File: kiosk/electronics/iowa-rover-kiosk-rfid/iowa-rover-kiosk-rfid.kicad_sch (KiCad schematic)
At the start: 6 parts, among them J1 Conn_01x04, J2 Conn_01x04, U1 ID12-LA, U2 ATtiny84-20P

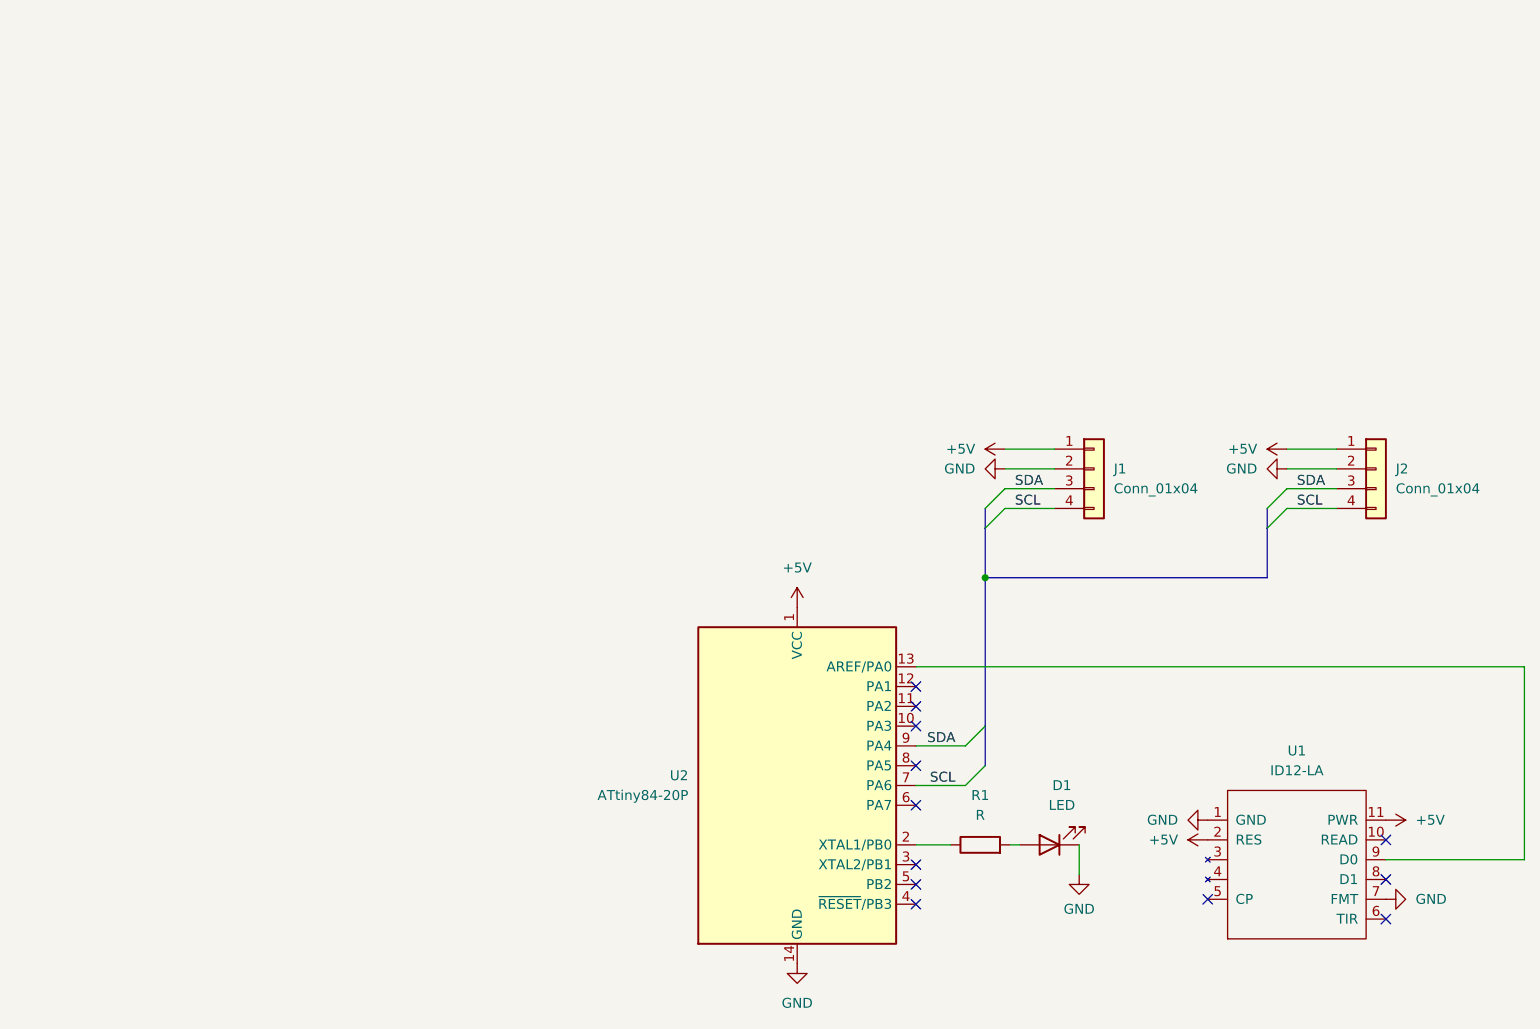
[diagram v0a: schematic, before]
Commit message: initial pass at board drawings
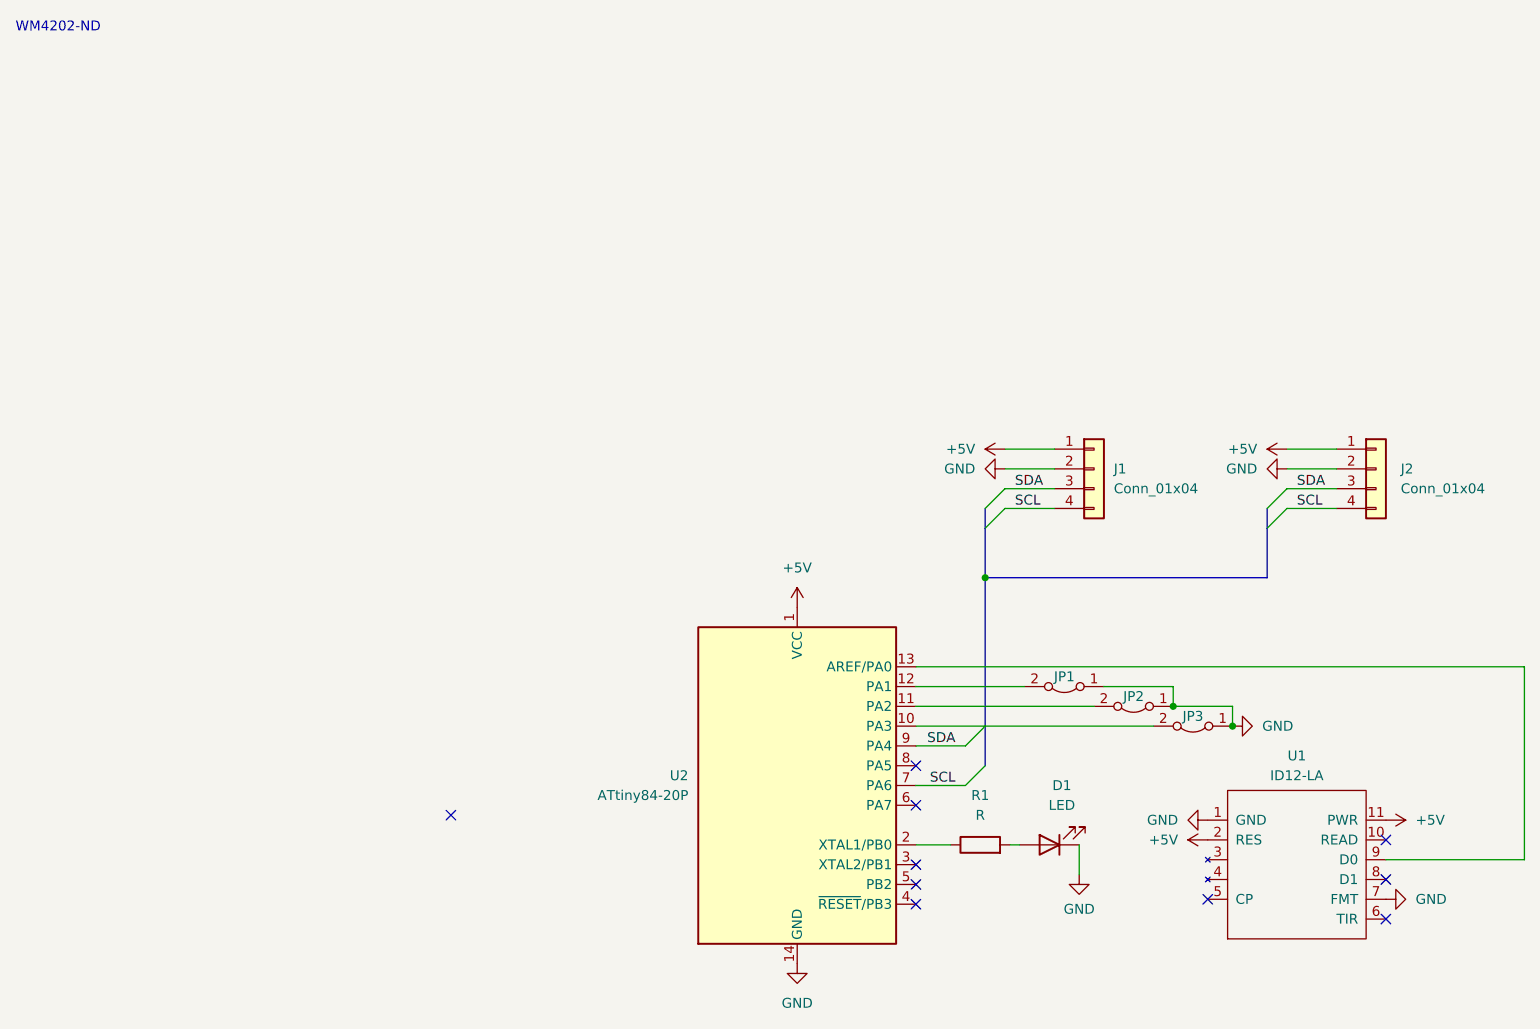
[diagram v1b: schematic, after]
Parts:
- added JP1, JP2, JP3: Jumper_2_Bridged, Jumper:SolderJumper-2_P1.3mm_Bridged_RoundedPad1.0x1.5mm, symbol Jumper:Jumper_2_Bridged
- D1: footprint (none) -> SMM:LED_D3.0mm
- J1, J2: footprint (none) -> SMM:KK-1x04
- R1: footprint (none) -> SMM:Resistor_L6.3mm_D2.5mm_P10.16mm_Horizontal
- U1: footprint (none) -> SMM:ID-12LA-Inverted
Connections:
- net GND: now also JP1.1 (A), JP2.1 (A), JP3.1 (A)
- net at U2.10 (PA3): now also JP3.2 (B)
- net at U2.11 (PA2): now also JP2.2 (B)
- net at U2.12 (PA1): now also JP1.2 (B)
- no-connect marks 12 -> 10
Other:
- note added: "WM4202-ND"
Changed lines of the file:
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@@
   (junction (at 124.46 72.39) (diameter 0) (color 0 0 0 0)
+  )
+  (junction (at 148.59 88.9) (diameter 0) (color 0 0 0 0)
+  )
+  (junction (at 156.21 91.44) (diameter 0) (color 0 0 0 0)
   )
   (no_connect (at 115.57 101.6))
@@
   (no_connect (at 175.895 116.205))
   (no_connect (at 115.57 109.22))
-  (no_connect (at 115.57 91.44))
   (no_connect (at 115.57 96.52))
   (no_connect (at 175.895 111.125))
-  (no_connect (at 115.57 88.9))
   (no_connect (at 153.035 113.665))
   (no_connect (at 115.57 114.3))
-  (no_connect (at 115.57 86.36))
   (no_connect (at 175.895 106.045))
+  (no_connect (at 55.88 102.87))
   (bus_entry (at 127 60.96) (size -2.54 2.54)
     (stroke (width 0) (type default))
@@
     (stroke (width 0) (type default))
   )
+  (wire (pts (xy 148.59 86.36) (xy 148.59 88.9))
+    (stroke (width 0) (type default))
+  )
   (wire (pts (xy 163.195 63.5) (xy 169.545 63.5))
     (stroke (width 0) (type default))
@@
     (stroke (width 0) (type default))
   )
+  (wire (pts (xy 138.43 88.9) (xy 115.57 88.9))
+    (stroke (width 0) (type default))
+  )
+  (wire (pts (xy 129.54 86.36) (xy 115.57 86.36))
+    (stroke (width 0) (type default))
+  )
   (wire (pts (xy 127 60.96) (xy 133.35 60.96))
     (stroke (width 0) (type default))
@@
     (stroke (width 0) (type default))
   )
+  (wire (pts (xy 156.21 88.9) (xy 156.21 91.44))
+    (stroke (width 0) (type default))
+  )
+  (wire (pts (xy 139.7 86.36) (xy 148.59 86.36))
+    (stroke (width 0) (type default))
+  )
   (bus (pts (xy 124.46 91.44) (xy 124.46 96.52))
     (stroke (width 0) (type default))
   )
+  (wire (pts (xy 124.46 91.44) (xy 115.57 91.44))
+    (stroke (width 0) (type default))
+  )
   (wire (pts (xy 120.015 106.68) (xy 115.57 106.68))
     (stroke (width 0) (type default))
@@
     (stroke (width 0) (type default))
   )
+  (wire (pts (xy 146.05 91.44) (xy 124.46 91.44))
+    (stroke (width 0) (type default))
+  )
+  (wire (pts (xy 148.59 88.9) (xy 156.21 88.9))
+    (stroke (width 0) (type default))
+  )
   (wire (pts (xy 163.195 60.96) (xy 169.545 60.96))
     (stroke (width 0) (type default))
@@
   (bus (pts (xy 160.655 63.5) (xy 160.655 66.04))
     (stroke (width 0) (type default))
+  )
+  (text "WM4202-ND" (at 0 2.54 0)
+    (effects (font (size 1.27 1.27)) (justify left bottom))
   )
   (label "SDA" (at 120.65 93.98 180) (fields_autoplaced)
@@
       (effects (font (size 1.27 1.27)))
     )
-    (property "Footprint" "" (at 123.825 108.458 90)
+    (property "Footprint" "SMM:Resistor_L6.3mm_D2.5mm_P10.16mm_Horizontal" (at 123.825 108.458 90)
       (effects (font (size 1.27 1.27)) hide)
     )
@@
       (effects (font (size 1.27 1.27)) (justify left))
     )
-    (property "Footprint" "" (at 138.43 58.42 0)
+    (property "Footprint" "SMM:KK-1x04" (at 138.43 58.42 0)
       (effects (font (size 1.27 1.27)) hide)
     )
@@
         (path "/9b7db916-9455-49c4-9ed6-a39496550f39"
           (reference "#PWR01") (unit 1)
+        )
+      )
+    )
+  )
+  (symbol (lib_id "power:GND") (at 156.21 91.44 90) (unit 1)
+    (in_bom yes) (on_board yes) (dnp no) (fields_autoplaced)
+    (property "Reference" "#PWR012" (at 162.56 91.44 0)
+      (effects (font (size 1.27 1.27)) hide)
+    )
+    (property "Value" "GND" (at 160.02 91.44 90)
+      (effects (font (size 1.27 1.27)) (justify right))
+    )
+    (property "Footprint" "" (at 156.21 91.44 0)
+      (effects (font (size 1.27 1.27)) hide)
+    )
+    (property "Datasheet" "" (at 156.21 91.44 0)
+      (effects (font (size 1.27 1.27)) hide)
+    )
+    (pin "1")
+    (instances
+      (project "iowa-rover-kiosk-rfid"
+        (path "/9b7db916-9455-49c4-9ed6-a39496550f39"
+          (reference "#PWR012") (unit 1)
         )
       )
@@
       (effects (font (size 1.27 1.27)))
     )
-    (property "Footprint" "" (at 132.715 106.68 0)
+    (property "Footprint" "SMM:LED_D3.0mm" (at 132.715 106.68 0)
       (effects (font (size 1.27 1.27)) hide)
     )
@@
   (symbol (lib_id "SMM:ID12-LA") (at 164.465 120.015 0) (unit 1)
     (in_bom yes) (on_board yes) (dnp no) (fields_autoplaced)
-    (property "Reference" "U1" (at 164.465 94.615 0)
-      (effects (font (size 1.27 1.27)))
-    )
-    (property "Value" "ID12-LA" (at 164.465 97.155 0)
-      (effects (font (size 1.27 1.27)))
-    )
-    (property "Footprint" "" (at 164.465 120.015 0)
+    (property "Reference" "U1" (at 164.465 95.25 0)
+      (effects (font (size 1.27 1.27)))
+    )
+    (property "Value" "ID12-LA" (at 164.465 97.79 0)
+      (effects (font (size 1.27 1.27)))
+    )
+    (property "Footprint" "SMM:ID-12LA-Inverted" (at 164.465 120.015 0)
       (effects (font (size 1.27 1.27)) hide)
     )
@@
     )
   )
+  (symbol (lib_id "Jumper:Jumper_2_Bridged") (at 151.13 91.44 180) (unit 1)
+    (in_bom yes) (on_board yes) (dnp no)
+    (property "Reference" "JP3" (at 151.13 90.17 0)
+      (effects (font (size 1.27 1.27)))
+    )
+    (property "Value" "Jumper_2_Bridged" (at 151.13 88.9 0)
+      (effects (font (size 1.27 1.27)) hide)
+    )
+    (property "Footprint" "Jumper:SolderJumper-2_P1.3mm_Bridged_RoundedPad1.0x1.5mm" (at 151.13 91.44 0)
+      (effects (font (size 1.27 1.27)) hide)
+    )
+    (property "Datasheet" "~" (at 151.13 91.44 0)
+      (effects (font (size 1.27 1.27)) hide)
+    )
+    (pin "1")
+    (pin "2")
+    (instances
+      (project "iowa-rover-kiosk-rfid"
+        (path "/9b7db916-9455-49c4-9ed6-a39496550f39"
+          (reference "JP3") (unit 1)
+        )
+      )
+    )
+  )
   (symbol (lib_id "power:GND") (at 127 58.42 270) (unit 1)
     (in_bom yes) (on_board yes) (dnp no) (fields_autoplaced)
@@
   (symbol (lib_id "Connector_Generic:Conn_01x04") (at 174.625 58.42 0) (unit 1)
     (in_bom yes) (on_board yes) (dnp no) (fields_autoplaced)
-    (property "Reference" "J2" (at 177.165 58.42 0)
-      (effects (font (size 1.27 1.27)) (justify left))
-    )
-    (property "Value" "Conn_01x04" (at 177.165 60.96 0)
-      (effects (font (size 1.27 1.27)) (justify left))
-    )
-    (property "Footprint" "" (at 174.625 58.42 0)
+    (property "Reference" "J2" (at 177.8 58.42 0)
+      (effects (font (size 1.27 1.27)) (justify left))
+    )
+    (property "Value" "Conn_01x04" (at 177.8 60.96 0)
+      (effects (font (size 1.27 1.27)) (justify left))
+    )
+    (property "Footprint" "SMM:KK-1x04" (at 174.625 58.42 0)
       (effects (font (size 1.27 1.27)) hide)
     )
@@
     )
   )
+  (symbol (lib_id "Jumper:Jumper_2_Bridged") (at 134.62 86.36 180) (unit 1)
+    (in_bom yes) (on_board yes) (dnp no)
+    (property "Reference" "JP1" (at 134.62 85.09 0)
+      (effects (font (size 1.27 1.27)))
+    )
+    (property "Value" "Jumper_2_Bridged" (at 134.62 83.82 0)
+      (effects (font (size 1.27 1.27)) hide)
+    )
+    (property "Footprint" "Jumper:SolderJumper-2_P1.3mm_Bridged_RoundedPad1.0x1.5mm" (at 134.62 86.36 0)
+      (effects (font (size 1.27 1.27)) hide)
+    )
+    (property "Datasheet" "~" (at 134.62 86.36 0)
+      (effects (font (size 1.27 1.27)) hide)
+    )
+    (pin "1")
+    (pin "2")
+    (instances
+      (project "iowa-rover-kiosk-rfid"
+        (path "/9b7db916-9455-49c4-9ed6-a39496550f39"
+          (reference "JP1") (unit 1)
+        )
+      )
+    )
+  )
   (symbol (lib_id "power:GND") (at 175.895 113.665 90) (unit 1)
     (in_bom yes) (on_board yes) (dnp no) (fields_autoplaced)
@@
         )
       )
+    )
+  )
+  (symbol (lib_id "Jumper:Jumper_2_Bridged") (at 143.51 88.9 180) (unit 1)
+    (in_bom yes) (on_board yes) (dnp no)
+    (property "Reference" "JP2" (at 143.51 87.63 0)
+      (effects (font (size 1.27 1.27)))
+    )
+    (property "Value" "Jumper_2_Bridged" (at 143.51 86.36 0)
+      (effects (font (size 1.27 1.27)) hide)
+    )
+    (property "Footprint" "Jumper:SolderJumper-2_P1.3mm_Bridged_RoundedPad1.0x1.5mm" (at 143.51 88.9 0)
+      (effects (font (size 1.27 1.27)) hide)
+    )
+    (property "Datasheet" "~" (at 143.51 88.9 0)
+      (effects (font (size 1.27 1.27)) hide)
+    )
+    (pin "1")
+    (pin "2")
+    (instances
+      (project "iowa-rover-kiosk-rfid"
+        (path "/9b7db916-9455-49c4-9ed6-a39496550f39"
+          (reference "JP2") (unit 1)
+        )
+      )

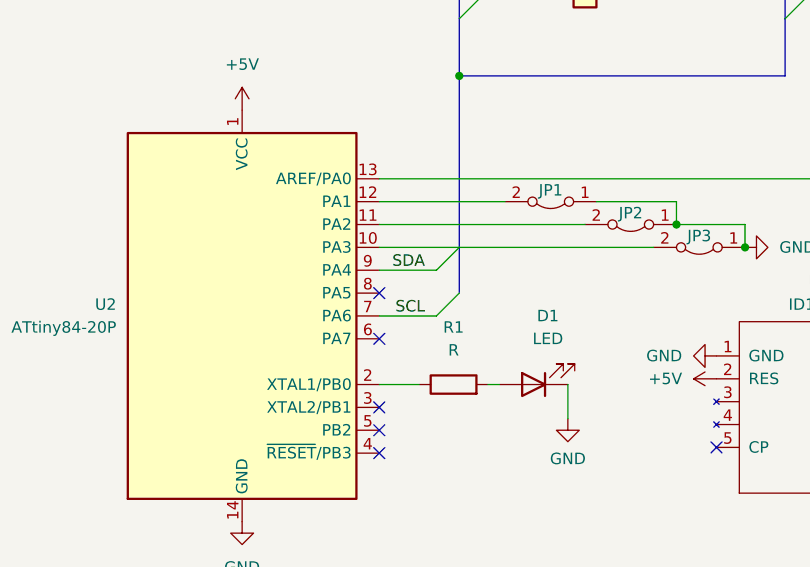
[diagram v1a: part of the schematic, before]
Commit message: fix sda/scl bus connections
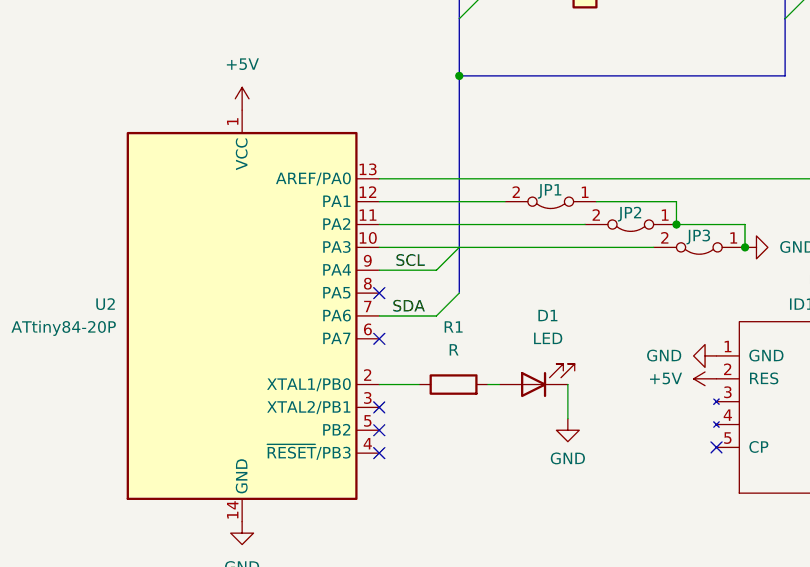
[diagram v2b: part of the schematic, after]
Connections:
- net SCL: now also U2.9 (PA4); no longer U2.7 (PA6)
- net SDA: now also U2.7 (PA6); no longer U2.9 (PA4)
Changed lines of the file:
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@@
     (effects (font (size 1.27 1.27)) (justify left bottom))
   )
-  (label "SDA" (at 120.65 93.98 180) (fields_autoplaced)
+  (label "SDA" (at 120.65 99.06 180) (fields_autoplaced)
     (effects (font (size 1.27 1.27)) (justify right bottom))
   )
@@
     (effects (font (size 1.27 1.27)) (justify left bottom))
   )
-  (label "SCL" (at 120.65 99.06 180) (fields_autoplaced)
+  (label "SCL" (at 120.65 93.98 180) (fields_autoplaced)
     (effects (font (size 1.27 1.27)) (justify right bottom))
   )

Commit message: add pdf schematics
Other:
- company: (none) -> Science Museum of Minnesota
- title: (none) -> Iowa Rover Kiosk - RFID Board
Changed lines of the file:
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@@
 (kicad_sch (version 20230121) (generator eeschema)
   (paper "A4")
+  (title_block
+    (title "Iowa Rover Kiosk - RFID Board")
+    (date "2023-10-05")
+    (rev "0")
+    (company "Science Museum of Minnesota")
+    (comment 1 "Kate Swanson")
+  )
   (junction (at 124.46 72.39) (diameter 0) (color 0 0 0 0)
   )
